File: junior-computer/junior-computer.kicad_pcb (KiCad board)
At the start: 2 copper layers, 217.2 x 113 mm, 81 parts, among them IC1 6502, IC10 74LS01, IC11 ULN2003, IC2 2708, IC3 6532, IC4 2114, IC5 2114, IC6 74LS145, IC7 74LS145, IC8 NE556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

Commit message: 'routing'
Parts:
- C7: footprint elektor:CAP-POL-2 -> elektor:CAP-POL-3
- moved R11 7.62 mm to (167.6, 44.5), turned to 180 degrees
- moved R13 7.62 mm to (167.6, 52.1), turned to 180 degrees
- moved C7 1.27 mm to (156.2, 48.3), turned to 90 degrees
- moved C11 1.27 mm to (39.4, 44.5), turned to 180 degrees
- turned C12 to 90 degrees
- turned C13 to 270 degrees
- turned C4 to 90 degrees
- turned R10 to 180 degrees
- turned R12 to 180 degrees
- turned R16 to 270 degrees
- turned R2 to 180 degrees
- turned R8 to 180 degrees
- turned R9 to 180 degrees
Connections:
- IC4 pad 1: A6 -> A0
- IC4 pad 15: A9 -> A8
- IC4 pad 16: A8 -> A4
- IC4 pad 17: A7 -> A3
- IC4 pad 2: A5 -> A1
- IC4 pad 3: A4 -> A2
- IC4 pad 4: A3 -> A9
- IC4 pad 5: A0 -> A5
- IC4 pad 6: A1 -> A6
- IC4 pad 7: A2 -> A7
- IC5 pad 1: A6 -> A0
- IC5 pad 15: A9 -> A8
- IC5 pad 16: A8 -> A4
- IC5 pad 17: A7 -> A3
- IC5 pad 2: A5 -> A1
- IC5 pad 3: A4 -> A2
- IC5 pad 4: A3 -> A9
- IC5 pad 5: A0 -> A5
- IC5 pad 6: A1 -> A6
- IC5 pad 7: A2 -> A7
- S1 pad 1: Net-(R17-Pad2) -> +5V
- S1 pad 2: +5V -> Net-(R17-Pad2)
- S2 pad 1: Net-(R19-Pad2) -> +5V
- S2 pad 2: +5V -> Net-(R19-Pad2)
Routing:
- net GNDD: track 2.54 -> 778.5 mm, vias 0 -> 1
- net +5V: track 0.00 -> 610.9 mm, vias 0 -> 1
- net PA1: track 0.00 -> 186.0 mm
- net PA0: track 0.00 -> 174.0 mm
- net Net-(IC7-Pad1): track 0.00 -> 129.5 mm
- net Net-(IC7-Pad3): track 0.00 -> 126.9 mm
- net A6: track 13.8 -> 120.0 mm
- net A11: track 0.00 -> 78.8 mm
- net Net-(IC7-Pad2): track 0.00 -> 76.0 mm
- net A12: track 0.00 -> 69.4 mm, vias 0 -> 1
- net PA2: track 0.00 -> 67.7 mm
- net PB2: track 0.00 -> 65.2 mm
- net PA4: track 0.00 -> 60.9 mm
- net A7: track 13.8 -> 73.3 mm
- net PA3: track 0.00 -> 59.1 mm
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
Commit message: routage complet
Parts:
- C12, C13: footprint elektor:CAP-POL-2 -> elektor:CAP-POL-1.5
- moved C13 0.90 mm to (127.6, 136.5)
- moved C12 0.64 mm to (124.5, 136.5)
- moved C5 0.64 mm to (102.2, 113.0), turned to 180 degrees
- moved D1 0.63 mm to (74.9, 134.0)
- turned R1 to 270 degrees
- turned R14 to 90 degrees
- turned R7 to 180 degrees
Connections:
- C10 pad 1: GNDD -> GND
- C11 pad 2: GNDD -> GND
- C12 pad 1: GNDD -> GND
- C13 pad 2: GNDD -> GND
- C14 pad 2: GNDD -> GND
- C2 pad 2: GNDD -> GND
- C3 pad 1: GNDD -> GND
- C4 pad 1: GNDD -> GND
- C5 pad 2: GNDD -> GND
- C6 pad 2: GNDD -> GND
- C7 pad 2: GNDD -> GND
- C8 pad 2: GNDD -> GND
- C9 pad 2: GNDD -> GND
- D2 pad 1: GNDD -> GND
- IC1 pad 1: GNDD -> GND
- IC1 pad 21: GNDD -> GND
- IC10 pad 14: (no net) -> +5V
- IC10 pad 7: (no net) -> GND
- IC11 pad 8: GNDD -> GND
- IC2 pad 12: GNDD -> GND
- IC3 pad 1: GNDD -> GND
- IC4 pad 11: D3 -> D0
- IC4 pad 12: D2 -> D1
- IC4 pad 13: D1 -> D2
- IC4 pad 14: D0 -> D3
- IC4 pad 9: GNDD -> GND
- IC5 pad 9: GNDD -> GND
- IC6 pad 8: GNDD -> GND
- IC7 pad 8: GNDD -> GND
- IC8 pad 7: GNDD -> GND
- IC9 pad 14: (no net) -> +5V
- IC9 pad 7: (no net) -> GND
- J2 pad A32: GNDD -> GND
- J2 pad A4: GNDD -> GND
- J2 pad C32: GNDD -> GND
- J2 pad C4: GNDD -> GND
- J3 pad 1: GNDD -> GND
- J4 pad 2: GNDD -> GND
- R18 pad 1: GNDD -> GND
- R20 pad 1: GNDD -> GND
- S25 pad 1: (no net) -> Net-(C2-Pad1)
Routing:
- net GND: track 0.00 -> 1013.8 mm, vias 0 -> 3
- net GNDD: track 778.5 -> 0.00 mm, vias 1 -> 0
- net NMI: track 0.00 -> 389.8 mm
- net PA2: track 67.7 -> 416.0 mm
- net PA3: track 59.1 -> 382.1 mm
- net PA6: track 54.5 -> 336.2 mm
- net PA5: track 52.6 -> 327.0 mm
- net PA4: track 60.9 -> 302.5 mm
- net +5V: track 610.9 -> 845.8 mm, vias 1 -> 2
- net RES: track 0.00 -> 230.5 mm, vias 0 -> 1
- net +12V: track 0.00 -> 221.4 mm, vias 0 -> 2
- net RAM.RW: track 14.8 -> 232.3 mm
- net PA1: track 186.0 -> 396.2 mm
- net PA0: track 174.0 -> 372.1 mm
- net Net-(IC10-Pad1): track 0.00 -> 198.0 mm
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
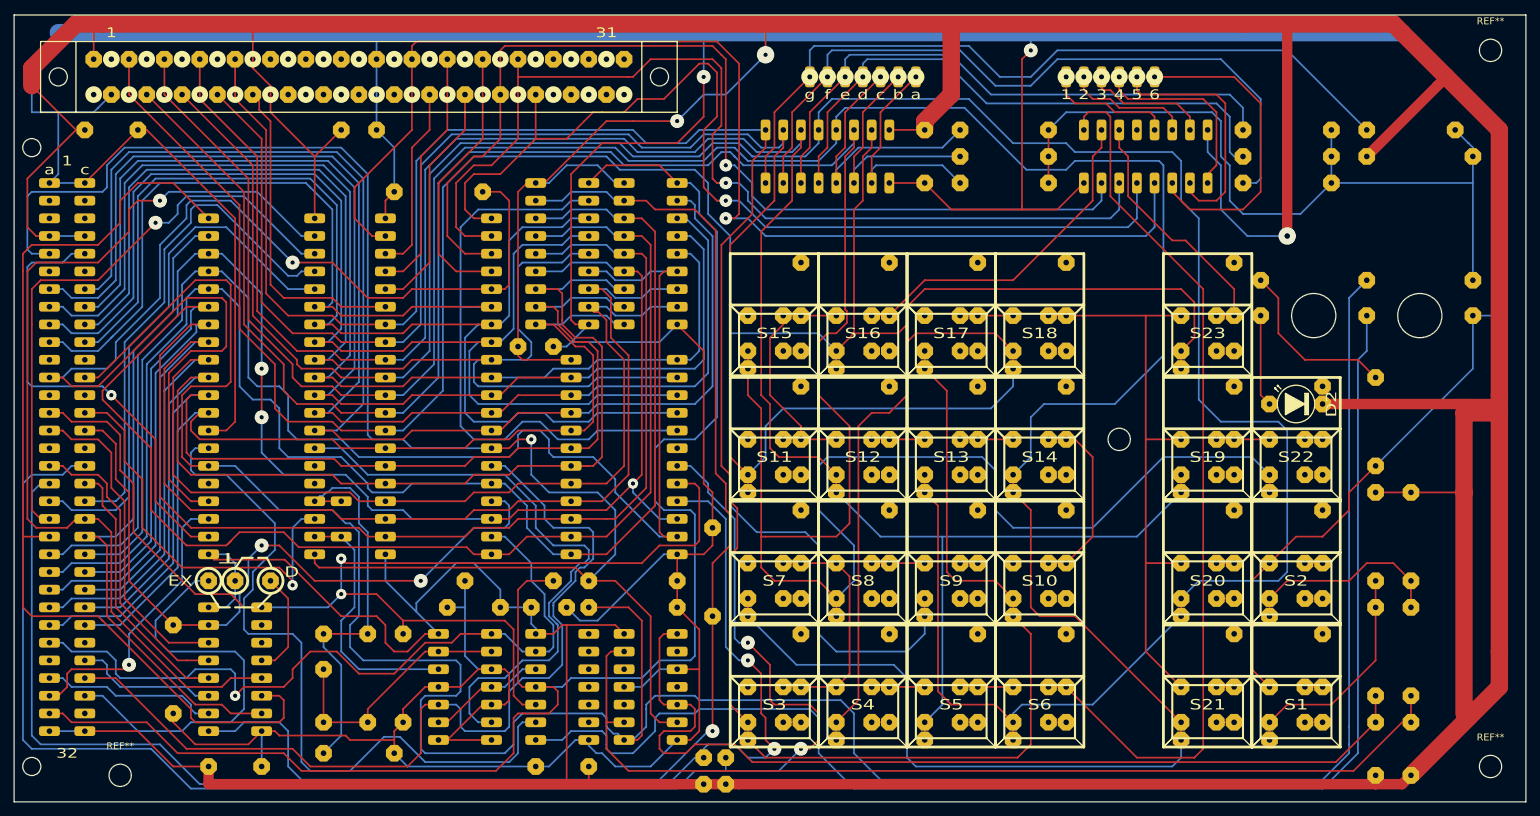
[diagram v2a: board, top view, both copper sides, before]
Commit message: amelioration dessin pistes
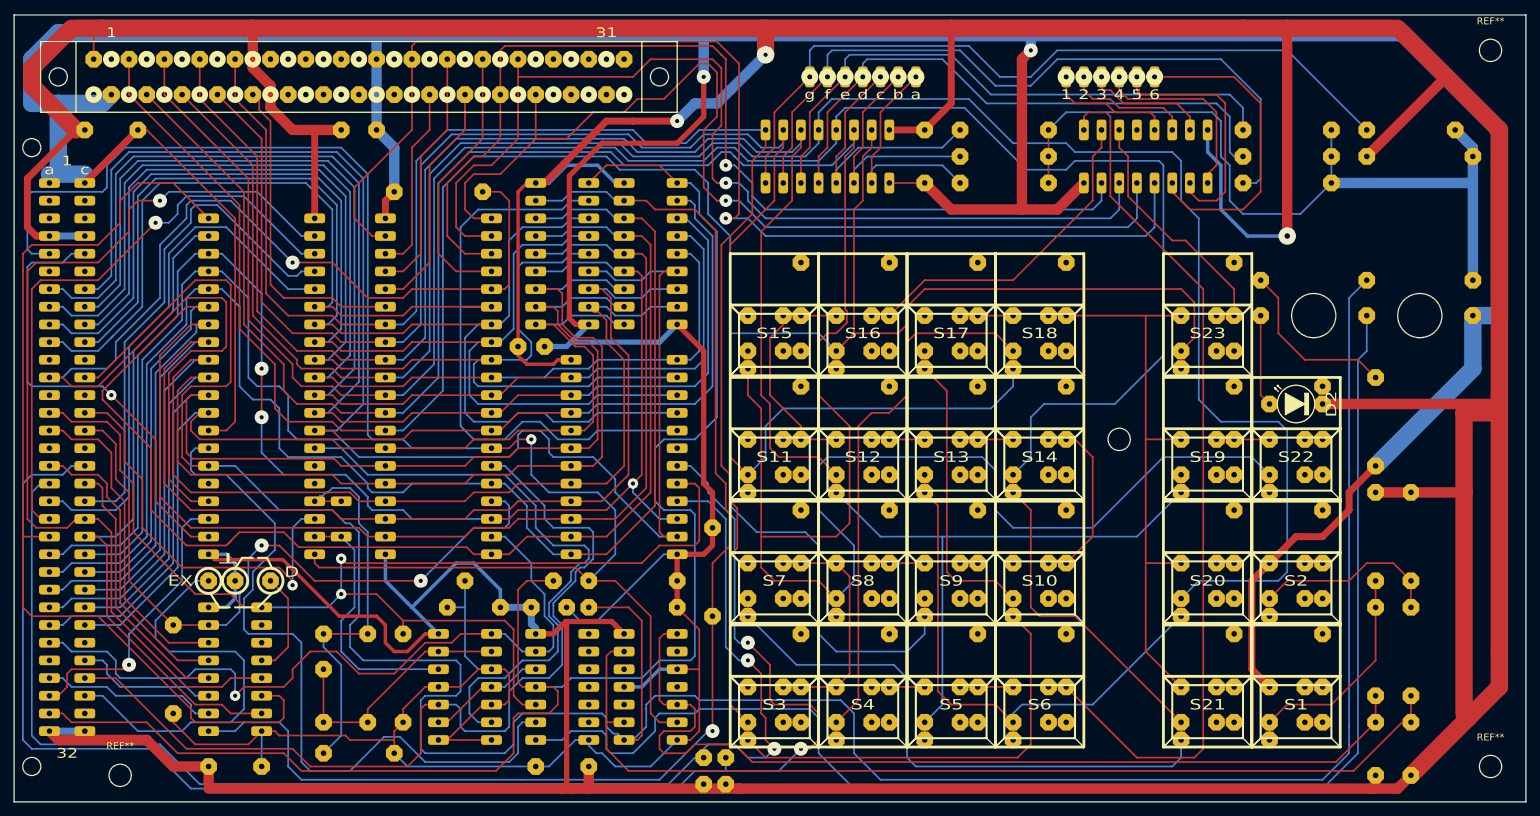
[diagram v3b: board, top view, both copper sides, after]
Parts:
- C8: footprint elektor:CAP-POL-2 -> elektor:CAP-POL-1.5
- moved C8 0.64 mm to (99.7, 75.6)
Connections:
- IC10 pad 7: GND -> (no net)
- IC9 pad 7: GND -> (no net)
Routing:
- net GND: track 1013.8 -> 1020.7 mm

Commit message: lettrage
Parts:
- added Ref**: Val**, elektor:lettrages2, F.Cu at (132.1, 81.3)
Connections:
- IC10 pad 7: (no net) -> GND
- IC9 pad 7: (no net) -> GND
- S25 pad 1: Net-(C2-Pad1) -> (no net)
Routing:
- net +5V: track 846.2 -> 847.5 mm

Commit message: modifs schema
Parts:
- removed C13: 1µ 16v, elektor:CAP-POL-1.5
- added D3: 1N4148, elektor:Diod-4, B.Cu at (230.5, 120.7)
- added J5: Conn_01x03_Female, elektor:K4-K6, F.Cu at (61.6, 120.7)
- added R21: 1k, elektor:Res-5, B.Cu at (119.4, 136.5)
- added R22: 1k, elektor:Res-5, B.Cu at (90.8, 136.5)
- added R23: 820k, elektor:Res-5, B.Cu at (231.1, 102.9)
- C12: value 1µ 16v -> 470n; footprint elektor:CAP-POL-1.5 -> elektor:CAP-2
- IC2: value 2708 -> 2716
- moved C12 113.0 mm to (228.6, 92.7), turned to 180 degrees
- moved C6 0.64 mm to (104.1, 136.5)
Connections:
- C12 pad 1: GND -> Net-(C12-Pad1)
- C12 pad 2: -5V -> +5V
- C2 pad 1: Net-(C2-Pad1) -> +5V
- IC10 pad 10: (no net) -> Net-(IC10-Pad10)
- IC10 pad 11: (no net) -> Net-(IC10-Pad10)
- IC10 pad 12: (no net) -> Net-(IC10-Pad10)
- IC10 pad 13: (no net) -> Net-(IC10-Pad13)
- IC10 pad 3: K7 -> Net-(IC10-Pad13)
- IC10 pad 4: RAM.RW -> +5V
- IC10 pad 8: (no net) -> Net-(IC10-Pad8)
- IC10 pad 9: (no net) -> K6
- IC2 pad 18: (no net) -> GND
- IC2 pad 19: +12V -> GND
- IC2 pad 21: -5V -> +5V
- IC4 pad 10: RAM.RW -> +5V
- IC5 pad 10: RAM.RW -> +5V
- J2 pad A31: RAM.RW -> +5V
- R10 pad 1: Net-(C2-Pad1) -> Net-(R10-Pad1)
- R11 pad 1: Net-(C2-Pad1) -> Net-(R10-Pad1)
- R12 pad 1: Net-(C2-Pad1) -> Net-(R10-Pad1)
- R13 pad 1: Net-(C2-Pad1) -> Net-(R10-Pad1)
- R5 pad 2: RAM.RW -> +5V
- R7 pad 1: Net-(C2-Pad1) -> Net-(R10-Pad1)
- R8 pad 1: Net-(C2-Pad1) -> Net-(R10-Pad1)
- R9 pad 1: Net-(C2-Pad1) -> Net-(R10-Pad1)
- S25 pad 1: (no net) -> Net-(R10-Pad1)
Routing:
- net +5V: track 847.5 -> 1117.9 mm
- net RAM.RW: track 232.3 -> 0.00 mm
- net +12V: track 221.4 -> 0.00 mm, vias 2 -> 0
- net -5V: track 198.0 -> 0.00 mm, vias 2 -> 0
- net Net-(R10-Pad1): track 0.00 -> 114.8 mm
- net Net-(C2-Pad1): track 113.7 -> 0.00 mm
- net Net-(IC10-Pad8): track 0.00 -> 87.0 mm, vias 0 -> 1
- net GND: track 1020.7 -> 1086.4 mm, vias 3 -> 6
- net K6: track 102.3 -> 161.9 mm, vias 2 -> 3
- net K7: track 172.5 -> 142.9 mm
- net Net-(C12-Pad1): track 0.00 -> 26.9 mm
- net Net-(IC10-Pad13): track 0.00 -> 21.4 mm
- net Net-(IC10-Pad10): track 0.00 -> 18.9 mm
- net K4: track 43.4 -> 58.6 mm
- net Net-(D3-Pad1): track 32.9 -> 46.4 mm
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
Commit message: correction empreintes
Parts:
- C12: footprint elektor:CAP-2 -> elektor:CAP-2-HEX
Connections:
- IC10 pad 4: +5V -> RAM.RW
- IC4 pad 10: +5V -> RAM.RW
- IC5 pad 10: +5V -> RAM.RW
- J2 pad A31: +5V -> RAM.RW
- R5 pad 2: +5V -> RAM.RW
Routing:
- net RAM.RW: track 0.00 -> 227.7 mm
- net +5V: track 1117.9 -> 897.4 mm
- net GND: track 1086.4 -> 1101.0 mm
- net Net-(D2-Pad2): track 13.2 -> 15.8 mm
- net PB1: track 146.8 -> 148.2 mm
- net PB2: track 147.3 -> 148.4 mm
- net PB4: track 174.9 -> 175.4 mm
- net Net-(C4-Pad2): track 140.9 -> 141.5 mm
- net Net-(C3-Pad2): track 138.2 -> 138.8 mm
